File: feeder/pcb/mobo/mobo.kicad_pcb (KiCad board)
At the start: 2 copper layers, 200 x 100 mm, 67 parts, among them J1 FTDI_HEADER, J2 PLATED_PADS, J3 SWD_10, M1 DRIVE_MOTOR, M2 PEEL_MOTOR, SW1 BUTTON_1, SW2 BUTTON_2, SW3 RESET, U1 TCS40DPR, U2 VCNT2020, U3 MAX3485, U4 DRV8833PWP, U5 AP1117-33, U6 STM32F103C8Tx, U7 MCP16301, U8 QRE1113, Y1 8MHz

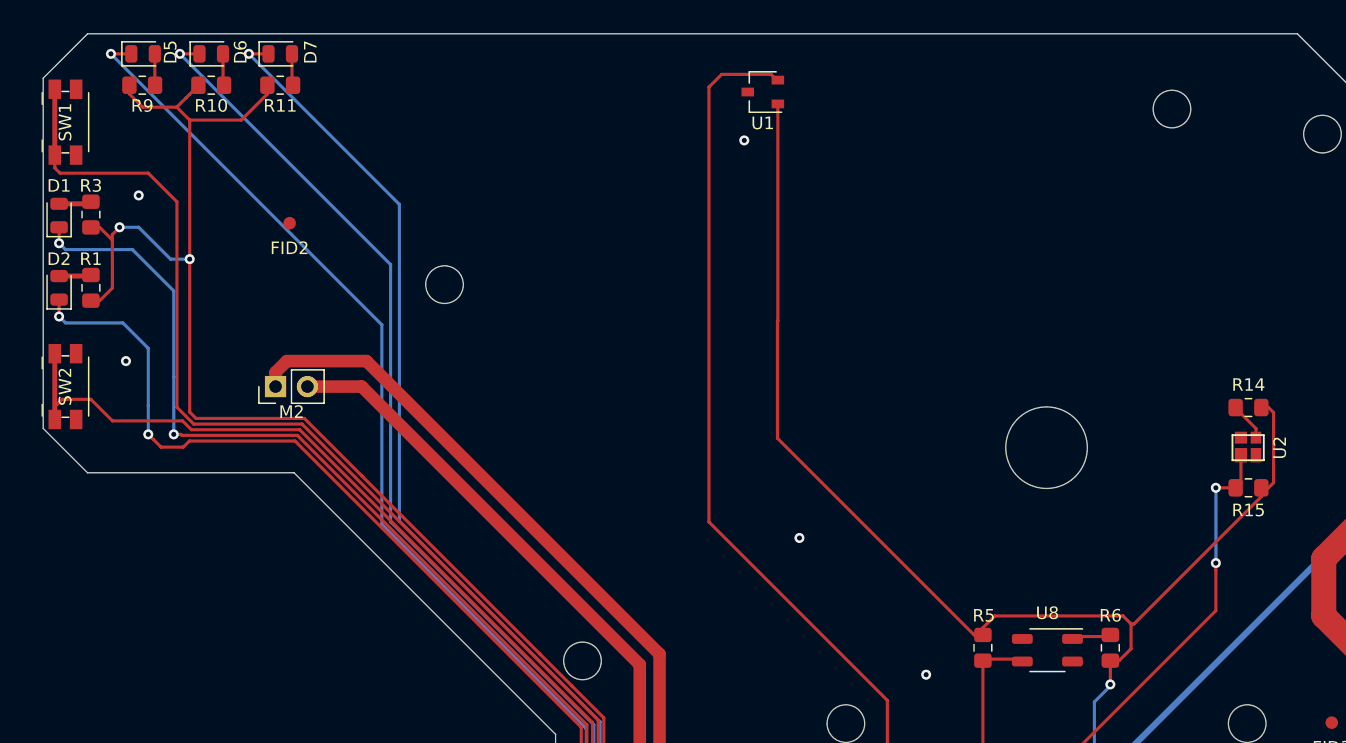
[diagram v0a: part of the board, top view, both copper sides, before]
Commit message: Updating the package "Resistor_SMD:R_0805_2012Metric_Pad1.15x1.40mm_HandSolder" to "Resistor_SMD:R_0805_2012Metric" as that makes everything consistent.
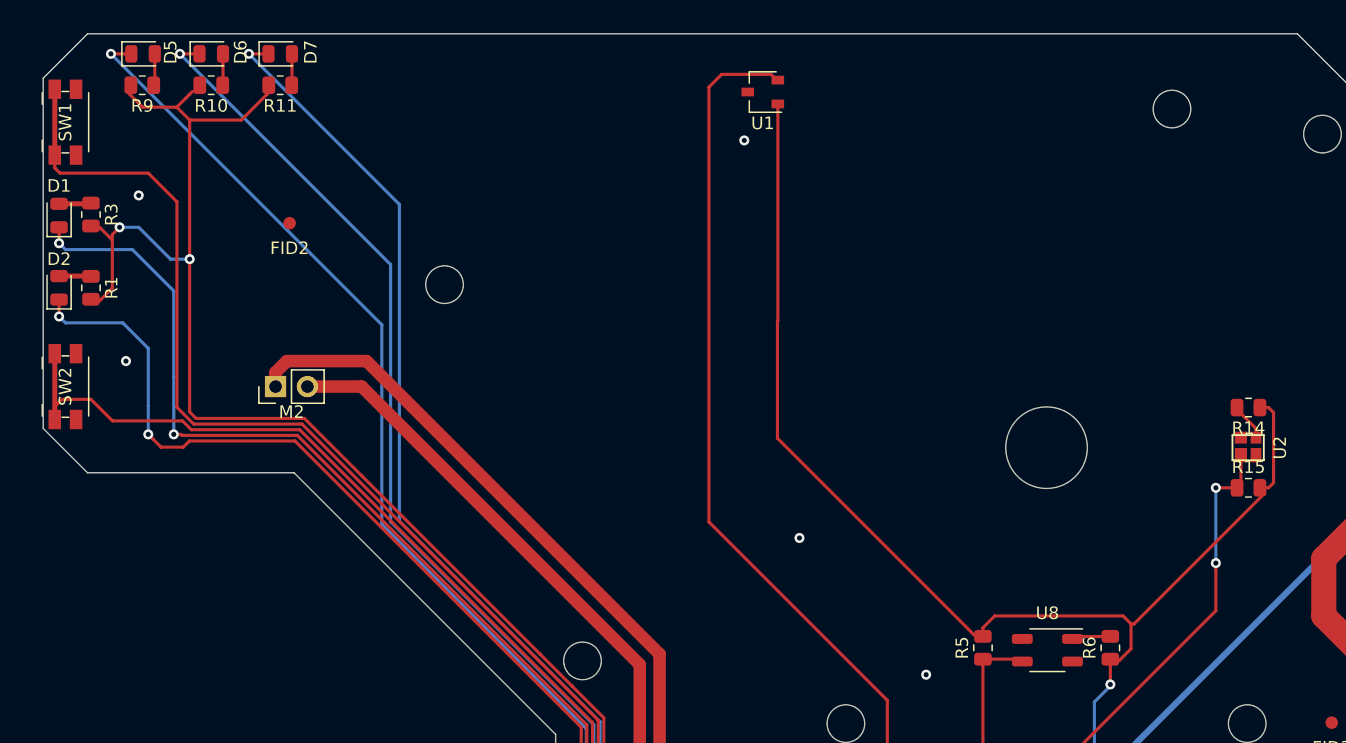
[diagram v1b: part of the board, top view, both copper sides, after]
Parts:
- R1, R10, R11, R14, R15, R3, R5, R6, R9: footprint Resistor_SMD:R_0805_2012Metric_Pad1.15x1.40mm_HandSolder -> Resistor_SMD:R_0805_2012Metric
